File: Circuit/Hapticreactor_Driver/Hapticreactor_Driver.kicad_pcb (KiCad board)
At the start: 2 copper layers, 31 x 18.8 mm, 21 parts, among them J1 Conn_01x02, J2 Conn_01x02, J3 Conn_01x02, U1 XIAO ESP32C3, U2 TB6552FNG_C_8_EL, U3 MCP4725xxx-xCH

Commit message: 秋野の回路に昇圧DCDCつけて東芝MDつけた
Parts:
- removed C1, C2: 0.1u, Capacitor_SMD:C_0603_1608Metric_Pad1.08x0.95mm_HandSolder
- removed J2: Conn_01x02, Connector_PinHeader_2.00mm:PinHeader_1x02_P2.00mm_Vertical
- added C3: 10uF, Capacitor_SMD:C_0603_1608Metric, B.Cu at (138.2, 69.0)
- added C4: 1uF, Capacitor_SMD:C_0603_1608Metric, B.Cu at (130.3, 69.0)
- added CIN1: 10uF, Capacitor_SMD:C_0603_1608Metric, B.Cu at (123.5, 73.4)
- added CL1: 10uF, Capacitor_SMD:C_0603_1608Metric, B.Cu at (124.3, 69.0)
- added D2: LED, LED_SMD:LED_0603_1608Metric, F.Cu at (144.0, 79.0)
- added D3: LED, LED_SMD:LED_0603_1608Metric, F.Cu at (141.7, 81.0)
- added D4: LED, LED_SMD:LED_0603_1608Metric, F.Cu at (140.7, 78.7)
- added R7: 1k, Resistor_SMD:R_0603_1608Metric_Pad0.98x0.95mm_HandSolder, B.Cu at (144.0, 79.1)
- added R8: 1k, Resistor_SMD:R_0603_1608Metric_Pad0.98x0.95mm_HandSolder, B.Cu at (141.6, 81.0)
- added R9: 1k, Resistor_SMD:R_0603_1608Metric_Pad0.98x0.95mm_HandSolder, B.Cu at (140.7, 78.3)
- added U4: ~, 0_MyFootprintLibrary:TA7291F, B.Cu at (138.5, 79.2)
- U2: value TB6552FNG_C_8_EL -> ~; footprint User:TB6552FNG -> 0_MyFootprintLibrary:XCL102D503CR-G
- moved U2 6.35 mm to (124.2, 71.3), turned to 0 degrees
- moved J1 5.98 mm to (141.6, 74.4)
- moved R5 5.04 mm to (124.7, 82.7), turned to -90 degrees
- moved R4 4.49 mm to (126.2, 82.0), turned to -90 degrees
- moved R2 4.46 mm to (120.0, 70.6), turned to 90 degrees
- moved C5 4.12 mm to (129.4, 81.3), turned to 180 degrees
- moved R1 3.88 mm to (120.0, 74.0)
- moved D1 3.11 mm to (143.0, 76.7), turned to 0 degrees
- moved U3 1.11 mm to (129.3, 84.2)
- moved JP1 0.40 mm to (132.6, 82.3)
- moved R3 0.40 mm to (133.2, 85.0)
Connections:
- U1 pad 11: /Motor_Driver/PWM_IN_B1 -> D10/GPIO10
- U1 pad 8: /Motor_Driver/PWM_IN_B2 -> D7/GPIO20
- U1 pad 9: unconnected-(U1-D8-Pad9) -> D8/GPIO8
- U2 pad 1: GND -> +BATT
- U2 pad 2: /Motor_Driver/PWM_IN_A1 -> GND
- U2 pad 3: /Motor_Driver/PWM_IN_A2 -> +5V
- U2 pad 4: /DAC/DAC_OUT -> GND
- U2 pad 5: +3.3V -> Net-(U2-L2)
- U2 pad 6: +BATT -> +5V
- U2 pad 7: /Motor_Driver/A_OUT_1 -> +BATT
- U2 pad 8: /Motor_Driver/A_OUT_2 -> Net-(U2-L2)
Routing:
- net GND: track 0.04 -> 47.5 mm, vias 24 -> 9
- net +5V: track 0.00 -> 25.9 mm, vias 0 -> 3
- net /Motor_Driver/B_OUT_2: track 20.4 -> 0.00 mm
- net /Motor_Driver/B_OUT_1: track 17.8 -> 0.00 mm
- net /Motor_Driver/PWM_IN_B2: track 17.3 -> 0.00 mm, vias 1 -> 0
- net /DAC/DAC_OUT: track 17.3 -> 5.72 mm, vias 0 -> 2
- net /Motor_Driver/PWM_IN_B1: track 9.48 -> 0.00 mm, vias 1 -> 0
- net D7/GPIO20: track 0.00 -> 9.23 mm, vias 0 -> 1
- net /Motor_Driver/A_OUT_2: track 17.4 -> 10.1 mm, vias 2 -> 0
- net /Motor_Driver/A_OUT_1: track 15.4 -> 9.17 mm, vias 2 -> 0
- net /XIAO_ESP32_C3/BATT_IN-: track 16.7 -> 22.0 mm
- net D8/GPIO8: track 0.00 -> 3.89 mm, vias 0 -> 1
- net D10/GPIO10: track 0.00 -> 3.51 mm, vias 0 -> 1
- net /DAC/DAC_SCL: track 13.7 -> 10.3 mm
- net +3.3V: track 17.6 -> 20.8 mm
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- added copper zone on B.Cu, net +BATT
- removed copper zone on B.Cu, net +3.3V
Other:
- board text added: "D10"
- board text added: "D7"
- board text added: "D8"
- board text added: "IN1,IN2"
- board text added: "LRA"
- board text removed: "A1 A2"
- board text removed: "B1 B2"
- board text removed: "D7,D10"
- board text removed: "PWM_A"
- board text removed: "PWM_B"

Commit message: ベタとかをちゃんとした．もう発注しても良さそう
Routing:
- net +BATT: track 22.6 -> 64.7 mm
- net +3.3V: track 20.8 -> 50.9 mm
- net GND: track 47.5 -> 56.8 mm, vias 9 -> 32
- added copper zone on F.Cu, net +3.3V
- added copper zone on B.Cu, net +5V
- added copper zone on F.Cu, net +5V

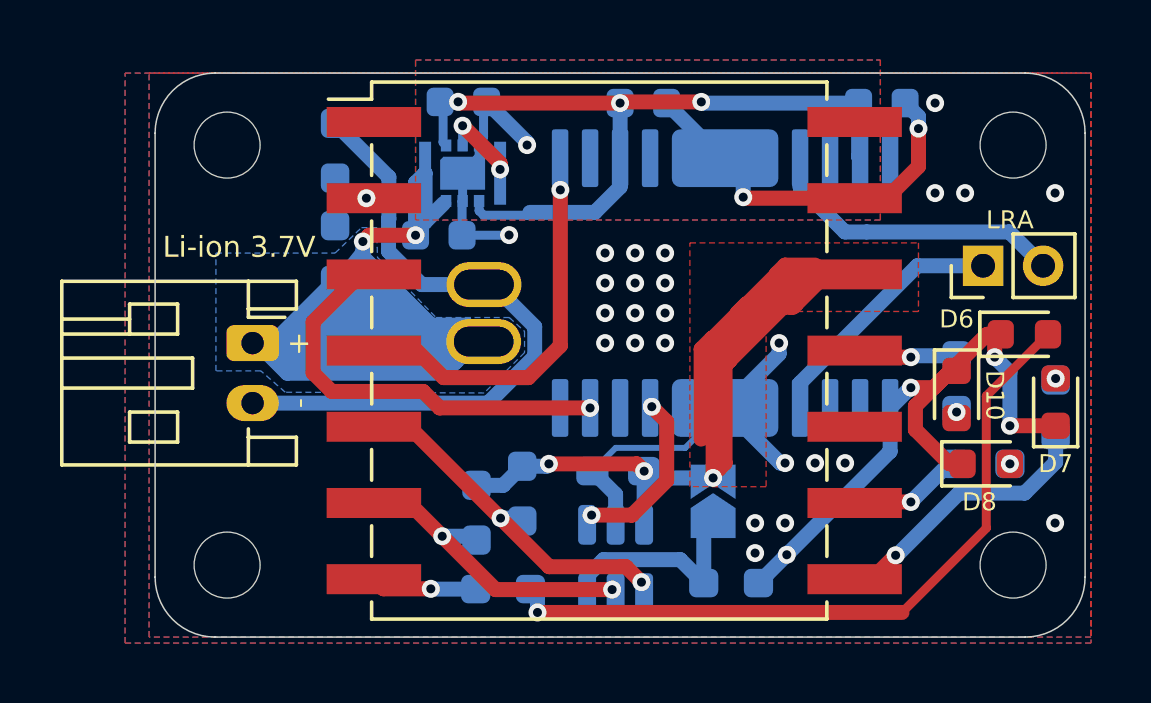
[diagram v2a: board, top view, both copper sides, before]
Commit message: スイッチを追加した．とりあえずこれで一旦発注しました
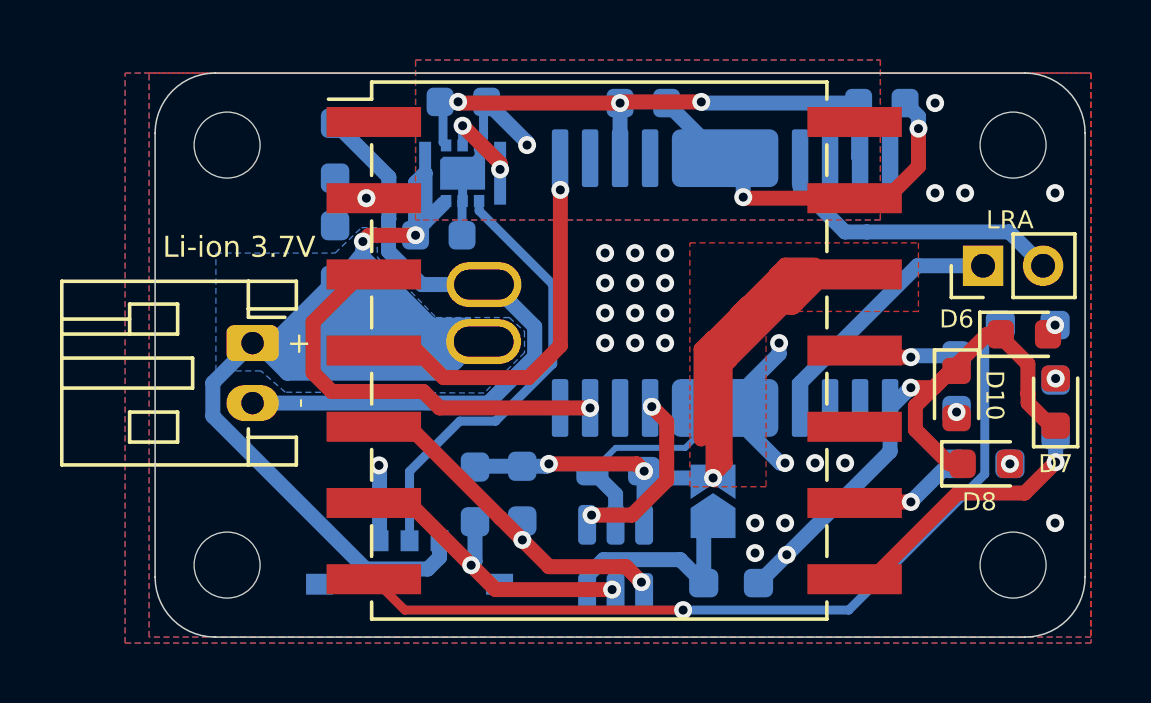
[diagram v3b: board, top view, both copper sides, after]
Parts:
- added SW2: SW_SPDT, 0_MyFootprintLibrary:SSAJ120100, B.Cu at (122.5, 84.9)
- moved R6 19.6 mm to (143.1, 76.4)
- moved R5 0.61 mm to (124.7, 82.0)
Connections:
- U2 pad 3: +5V -> Net-(SW2-B)
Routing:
- net /XIAO_ESP32_C3/D6/GPIO6: track 3.53 -> 27.8 mm
- net Net-(D1-A): track 24.3 -> 0.00 mm
- net Net-(SW2-B): track 0.00 -> 15.0 mm
- net +BATT: track 64.7 -> 78.1 mm
- net +5V: track 25.9 -> 19.4 mm
- net GND: vias 32 -> 30
